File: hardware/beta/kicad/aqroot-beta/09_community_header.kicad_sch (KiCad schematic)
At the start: 0 parts

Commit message: AQROOT Beta: finish power-tree integration and add community-header connector map
01_POWER_TREE:
- Wire MAX17048 fuel gauge (U14): VDD/CELL to BAT_PROTECTED_P, GND/EP/CTG
  to GND, SCL to I2C_SCL_INT, SDA to I2C_SDA_INT, QSTRT no-connect.
- Add C36 bulk cap on BAT_PROTECTED_P and TP11 test point on MAX17048_ALRT_N.
- Add 8 hierarchical labels: USB_D_N_MCU, USB_D_P_MCU, I2C_SDA_INT,
  I2C_SCL_INT, NFC_5V_EN, NFC_5V_PA_PENDING, BQ25185_SYS, BAT_PROTECTED_P.

Root sheet:
- Import the 8 matching 01_POWER_TREE sheet pins and name six of them at
  root level, promoting BQ25185_SYS, BAT_PROTECTED_P, NFC_5V_EN,
  USB_D_N_MCU and USB_D_P_MCU from sheet-local to root nets.

09_COMMUNITY_HEADER:
- Add J5 (Conn_02x13_Odd_Even, PinHeader_2x13_P2.54mm_Vertical) with the
  full 26-pin map, plus orientation and 3.3V-only warning notes.

04_SPI_B_RADIOS_NFC:
- KiCad de-duplicated two colliding pin UUIDs on C19 (the file carried each
  UUID twice); included because it is a file-integrity fix, no design change.

Known incomplete, carried forward:
- Root sheet pins I2C_SDA_INT and NFC_5V_PA_PENDING are imported but not
  wired, so MAX17048 SDA sits on an isolated sheet-local net while SCL is
  bonded. Fuel-gauge I2C is not yet electrically complete.
- Community header nets are sheet-local only; 09_COMMUNITY_HEADER has no
  root sheet pins, and the 100R series / ESD parts named in its notes do
  not exist yet.
- Not ERC-clean and not fabrication-ready.

Co-Authored-By: Claude Opus 5 <noreply@anthropic.com>
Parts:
- added J5: COMMUNITY_HEADER_2x13, Connector_PinHeader_2.54mm:PinHeader_2x13_P2.54mm_Vertical, symbol Connector_Generic:Conn_02x13_Odd_Even
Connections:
- new net +3V3: J5.1 (Pin_1)
- new net ACC_3V3_SW: J5.26 (Pin_26)
- new net FAST_IO_GPIO43_HDR: J5.23 (Pin_23)
- new net GND: J5.13 (Pin_13), J5.2 (Pin_2), J5.20 (Pin_20), J5.25 (Pin_25), J5.7 (Pin_7)
- new net I2C_SCL_EXT_HDR: J5.22 (Pin_22)
- new net I2C_SDA_EXT_HDR: J5.21 (Pin_21)
- new net WAKE_ATTN_N_HDR: J5.24 (Pin_24)
- new net XGPIO0_HDR: J5.3 (Pin_3)
- new net XGPIO10_HDR: J5.15 (Pin_15)
- new net XGPIO11_HDR: J5.16 (Pin_16)
- new net XGPIO12_HDR: J5.17 (Pin_17)
- new net XGPIO13_HDR: J5.18 (Pin_18)
- new net XGPIO14_HDR: J5.19 (Pin_19)
- new net XGPIO1_HDR: J5.4 (Pin_4)
- new net XGPIO2_HDR: J5.5 (Pin_5)
- new net XGPIO3_HDR: J5.6 (Pin_6)
- new net XGPIO4_HDR: J5.8 (Pin_8)
- new net XGPIO5_HDR: J5.9 (Pin_9)
- new net XGPIO6_HDR: J5.10 (Pin_10)
- new net XGPIO7_HDR: J5.11 (Pin_11)
- new net XGPIO8_HDR: J5.12 (Pin_12)
- new net XGPIO9_HDR: J5.14 (Pin_14)
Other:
- note added: "COMMUNITY HEADER - 2×13, 2.54 mm PIN 1 = +3V3 ODD PINS = LEFT COLUMN EVEN PINS = RIGHT COLUMN TOP TO BOTTOM BETA CONNECTOR IS NOT KEYED ADD PIN-1 TRIANGLE ON SILKSCREEN PRODUCTION UPGRADE: SHROUDED / KEYED CONNECTOR"
- note added: "COMMUNITY HEADER LOGIC = 3.3V ONLY NO 5V-TOLERANCE CLAIM NO 5V PASSTHROUGH ALL XGPIO LINES: 100R SERIES + CONNECTOR-SIDE ESD"

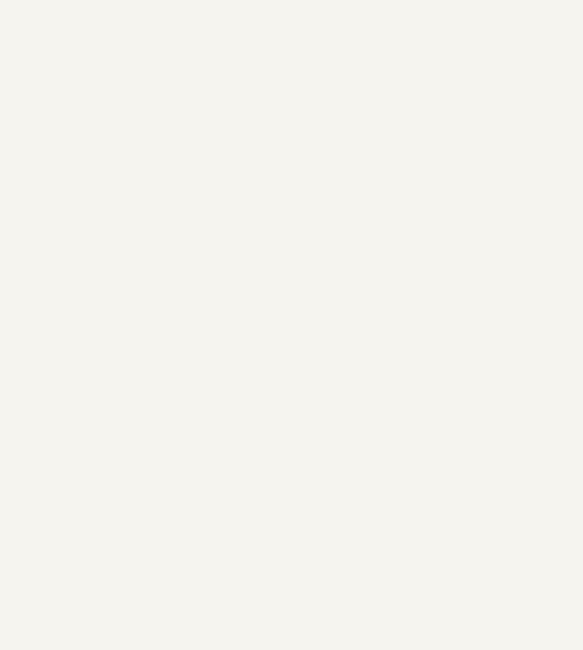
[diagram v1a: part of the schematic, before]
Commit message: AQROOT Beta: expose community-header internal hierarchy
09_COMMUNITY_HEADER:
- Add 20 hierarchical labels declaring the sheet's interface: XGPIO0-XGPIO14
  (bidirectional), I2C_SDA_INT (bidirectional), I2C_SCL_INT (input),
  ACC_PWR_EN (input), FAST_IO_U0TXD_ROOTPROBE_CS (input) and WAKE_INT_N
  (output). Purely additive: 220 insertions, 0 deletions.
- The existing connector-side local labels (XGPIO0_HDR-XGPIO14_HDR,
  I2C_SDA_EXT_HDR, I2C_SCL_EXT_HDR, FAST_IO_GPIO43_HDR, WAKE_ATTN_N_HDR,
  ACC_3V3_SW) are untouched.

Root sheet:
- Add the 20 matching sheet pins to the 09_COMMUNITY_HEADER sheet symbol.

This exposes the interface only. It does not connect anything:

- All 20 new root sheet pins are PLACED BUT UNWIRED. None carries a root
  wire, none has a matching root label, and none shares a net with any
  other sheet pin. Root pins still require wiring.
- The 20 new hierarchical labels inside 09 are likewise not attached to any
  wire, so they do not yet meet the *_HDR connector nets.
- J5 protection circuitry is not captured yet. The sheet notes call for
  100R series resistors and connector-side ESD on every XGPIO line; those
  parts do not exist, and they are what should eventually bridge XGPIO<n>
  to XGPIO<n>_HDR.

Verified with kicad-cli netlist export: this commit changes zero
connectivity. 145 nets and 433 pins before and after, with no pin changing
net. ERC rises 217 -> 257 violations, exactly +20 pin_not_connected and
+20 label_dangling, one of each per declared signal.

Not ERC-clean. Not fabrication-ready.

Co-Authored-By: Claude Opus 5 <noreply@anthropic.com>
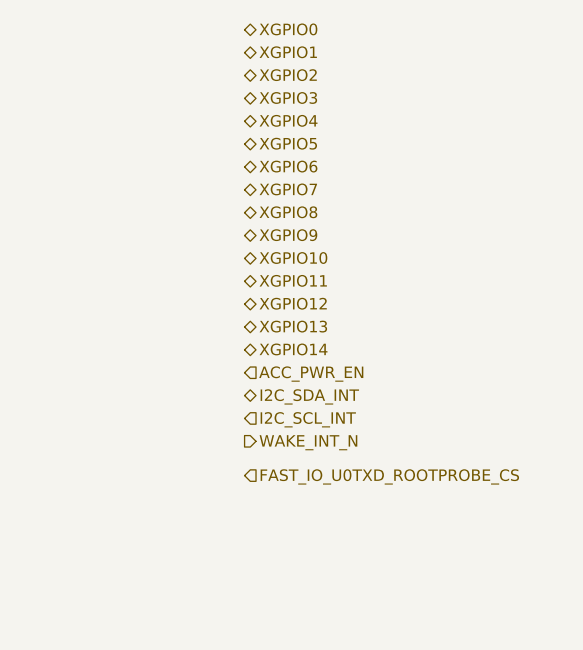
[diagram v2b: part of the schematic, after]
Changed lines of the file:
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@@
+		)
+	)
+	(hierarchical_label "XGPIO6"
+		(shape bidirectional)
+		(at 251.46 44.45 0)
+		(effects
+			(font
+				(size 1.27 1.27)
+			)
+			(justify left)
+		)
+	)
+	(hierarchical_label "XGPIO11"
+		(shape bidirectional)
+		(at 251.46 57.15 0)
+		(effects
+			(font
+				(size 1.27 1.27)
+			)
+			(justify left)
+		)
+	)
+	(hierarchical_label "I2C_SCL_INT"
+		(shape input)
+		(at 251.46 72.39 0)
+		(effects
+			(font
+				(size 1.27 1.27)
+			)
+			(justify left)
+		)
+	)
+	(hierarchical_label "XGPIO1"
+		(shape bidirectional)
+		(at 251.46 31.75 0)
+		(effects
+			(font
+				(size 1.27 1.27)
+			)
+			(justify left)
+		)
+	)
+	(hierarchical_label "XGPIO8"
+		(shape bidirectional)
+		(at 251.46 49.53 0)
+		(effects
+			(font
+				(size 1.27 1.27)
+			)
+			(justify left)
+		)
+	)
+	(hierarchical_label "XGPIO13"
+		(shape bidirectional)
+		(at 251.46 62.23 0)
+		(effects
+			(font
+				(size 1.27 1.27)
+			)
+			(justify left)
+		)
+	)
+	(hierarchical_label "I2C_SDA_INT"
+		(shape bidirectional)
+		(at 251.46 69.85 0)
+		(effects
+			(font
+				(size 1.27 1.27)
+			)
+			(justify left)
+		)
+	)
+	(hierarchical_label "XGPIO7"
+		(shape bidirectional)
+		(at 251.46 46.99 0)
+		(effects
+			(font
+				(size 1.27 1.27)
+			)
+			(justify left)
+		)
+	)
+	(hierarchical_label "XGPIO2"
+		(shape bidirectional)
+		(at 251.46 34.29 0)
+		(effects
+			(font
+				(size 1.27 1.27)
+			)
+			(justify left)
+		)
+	)
+	(hierarchical_label "XGPIO0"
+		(shape bidirectional)
+		(at 251.46 29.21 0)
+		(effects
+			(font
+				(size 1.27 1.27)
+			)
+			(justify left)
+		)
+	)
+	(hierarchical_label "ACC_PWR_EN"
+		(shape input)
+		(at 251.46 67.31 0)
+		(effects
+			(font
+				(size 1.27 1.27)
+			)
+			(justify left)
+		)
+	)
+	(hierarchical_label "XGPIO10"
+		(shape bidirectional)
+		(at 251.46 54.61 0)
+		(effects
+			(font
+				(size 1.27 1.27)
+			)
+			(justify left)
+		)
+	)
+	(hierarchical_label "FAST_IO_U0TXD_ROOTPROBE_CS"
+		(shape input)
+		(at 251.46 78.74 0)
+		(effects
+			(font
+				(size 1.27 1.27)
+			)
+			(justify left)
+		)
+	)
+	(hierarchical_label "XGPIO9"
+		(shape bidirectional)
+		(at 251.46 52.07 0)
+		(effects
+			(font
+				(size 1.27 1.27)
+			)
+			(justify left)
+		)
+	)
+	(hierarchical_label "XGPIO5"
+		(shape bidirectional)
+		(at 251.46 41.91 0)
+		(effects
+			(font
+				(size 1.27 1.27)
+			)
+			(justify left)
+		)
+	)
+	(hierarchical_label "XGPIO14"
+		(shape bidirectional)
+		(at 251.46 64.77 0)
+		(effects
+			(font
+				(size 1.27 1.27)
+			)
+			(justify left)
+		)
+	)
+	(hierarchical_label "WAKE_INT_N"
+		(shape output)
+		(at 251.46 74.93 0)
+		(effects
+			(font
+				(size 1.27 1.27)
+			)
+			(justify left)
+		)
+	)
+	(hierarchical_label "XGPIO3"
+		(shape bidirectional)
+		(at 251.46 36.83 0)
+		(effects
+			(font
+				(size 1.27 1.27)
+			)
+			(justify left)
+		)
+	)
+	(hierarchical_label "XGPIO12"
+		(shape bidirectional)
+		(at 251.46 59.69 0)
+		(effects
+			(font
+				(size 1.27 1.27)
+			)
+			(justify left)
+		)
+	)
+	(hierarchical_label "XGPIO4"
+		(shape bidirectional)
+		(at 251.46 39.37 0)
+		(effects
+			(font
+				(size 1.27 1.27)
+			)
+			(justify left)
 		)
 	)

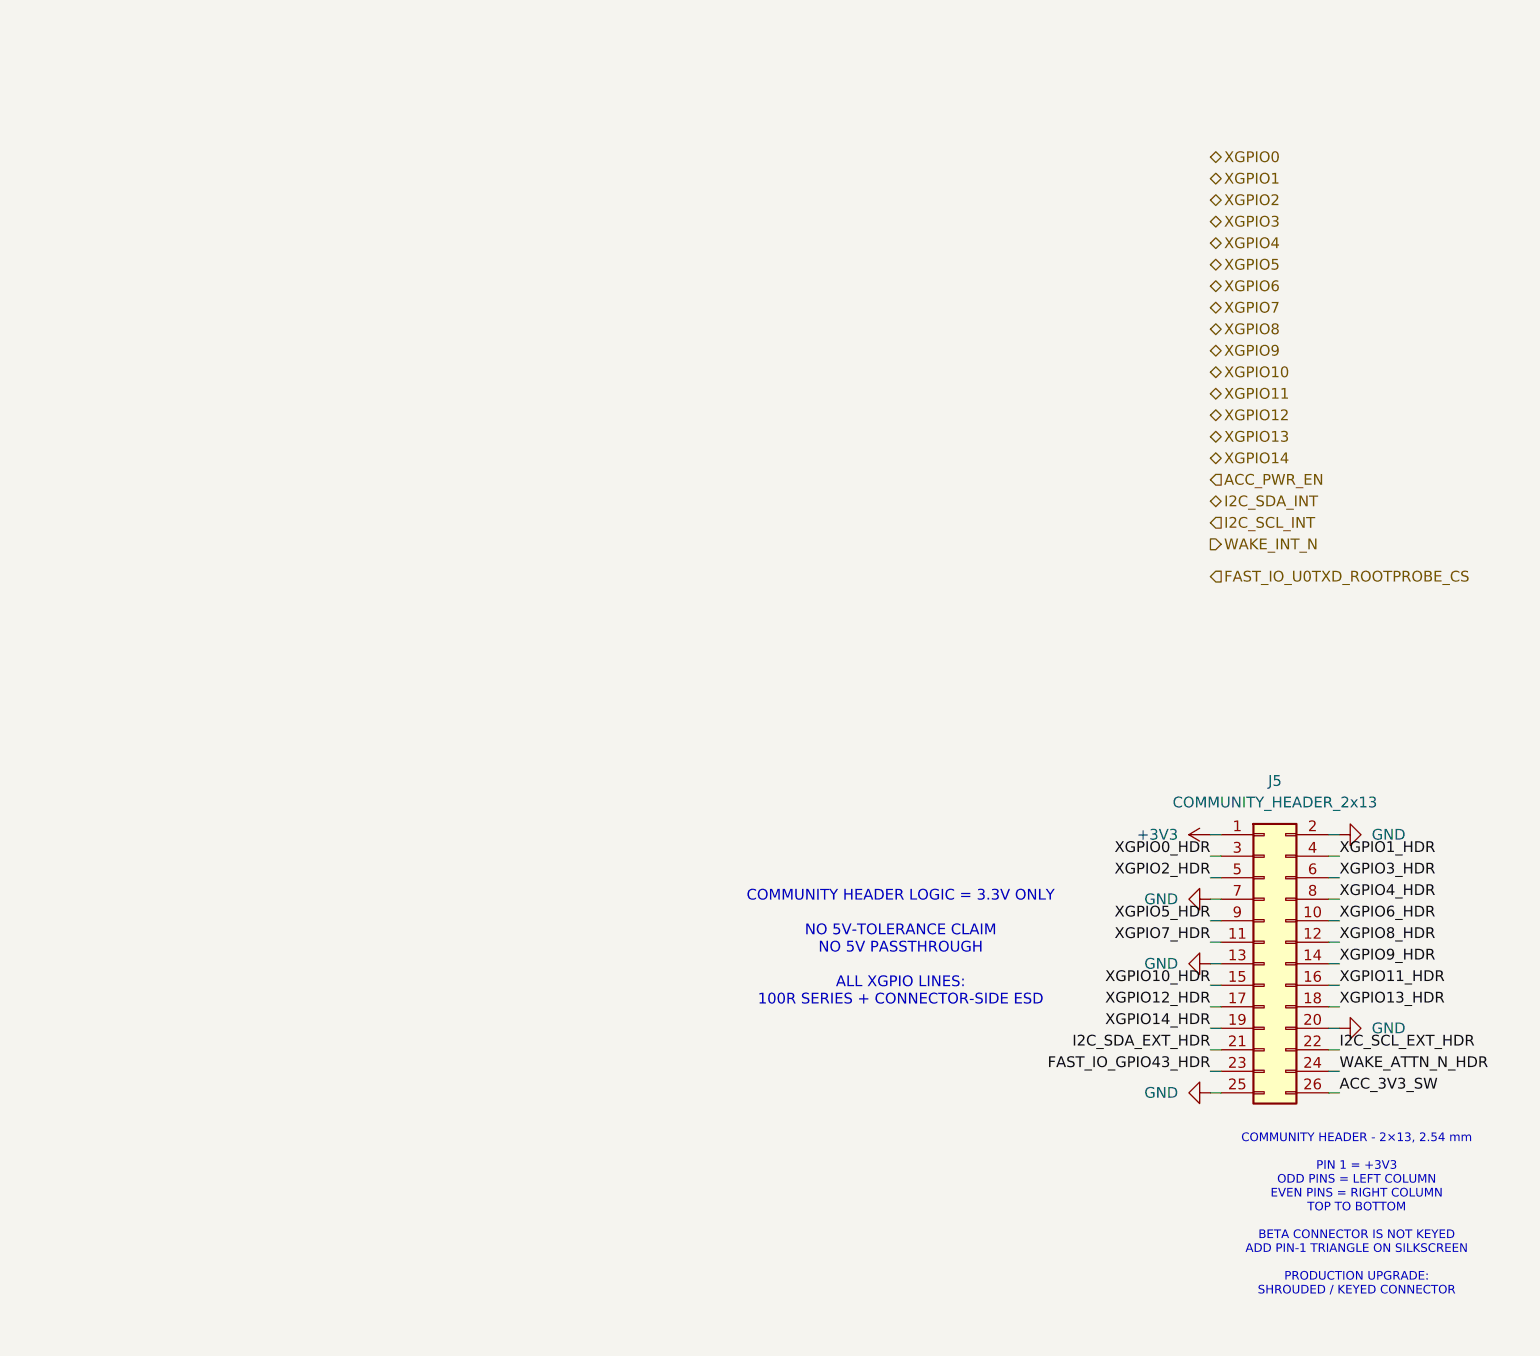
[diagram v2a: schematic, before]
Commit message: AQROOT Beta: add accessory power and protected external I2C
Checkpoint of the 09_COMMUNITY_HEADER accessory-power and protected external
I2C milestone. Verified with a scratch kicad-cli netlist export and ERC.

Confirmed as designed:
- TPS22918 (U15): VIN=+3V3, ON=ACC_PWR_EN, GND=GND, VOUT on the accessory rail.
  C37 1uF +3V3->GND, C38 1uF rail->GND, C39 100nF CT->GND, R46 100k QOD->rail,
  TP12 on rail.
- TCA9517A (U16): VCCA=+3V3, VCCB=rail, EN=ACC_PWR_EN, SCLA=I2C_SCL_INT,
  SDAA=I2C_SDA_INT. C40 100nF +3V3->GND, C42 100nF rail->GND.
- R47 22R from SCLB to I2C_SCL_EXT_HDR; R48 22R from SDAB to I2C_SDA_EXT_HDR.
- TPD2E009DBZR (D2): IO1 on I2C_SCL_EXT_HDR, IO2 on I2C_SDA_EXT_HDR, GND on
  GND. SDA and SCL confirmed as distinct nets.
- R49 4.7k between rail and I2C_SDA_EXT_HDR; R50 4.7k between rail and
  I2C_SCL_EXT_HDR.
- The accessory rail is a single correctly wired 9-node net: U15.6, U16.8,
  C38.1, C42.2, R46.2, R49.2, R50.2, TP12.1, J5.26.

Defects found during verification, NOT fixed in this commit:
- An empty label, (label "") at (273.05, 99.06), is attached to the accessory
  rail. KiCad resolves the name to the empty string in preference to
  ACC_3V3_SW, so the rail exports as <NO NET> and the ACC_3V3_SW name does not
  exist in the netlist. ERC reports this as multiple_net_names. Wiring is
  correct; only the net name is lost.
- U16 pin 4 (GND, power input) is not connected to board GND. It reaches GND
  only through C41 in series, on the local net Net-(U16-GND) = {U16.4, C41.2}.
- R49 and R50 do not have the KiCad (dnp yes) property set. "DNP" appears only
  in their Value strings, so they are not flagged as do-not-populate.
- 12 of the 16 parts on this sheet have no footprint assigned: C37-C42, R46-R50
  and TP12. Only D2, J5, U15 and U16 are footprinted.

Known incomplete, as expected at this milestone:
- XGPIO0-14 resistor/ESD blocks not captured
- WAKE protection not captured (J5.24 sits on a local WAKE_ATTN_N_HDR net)
- FAST_IO protection not capt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
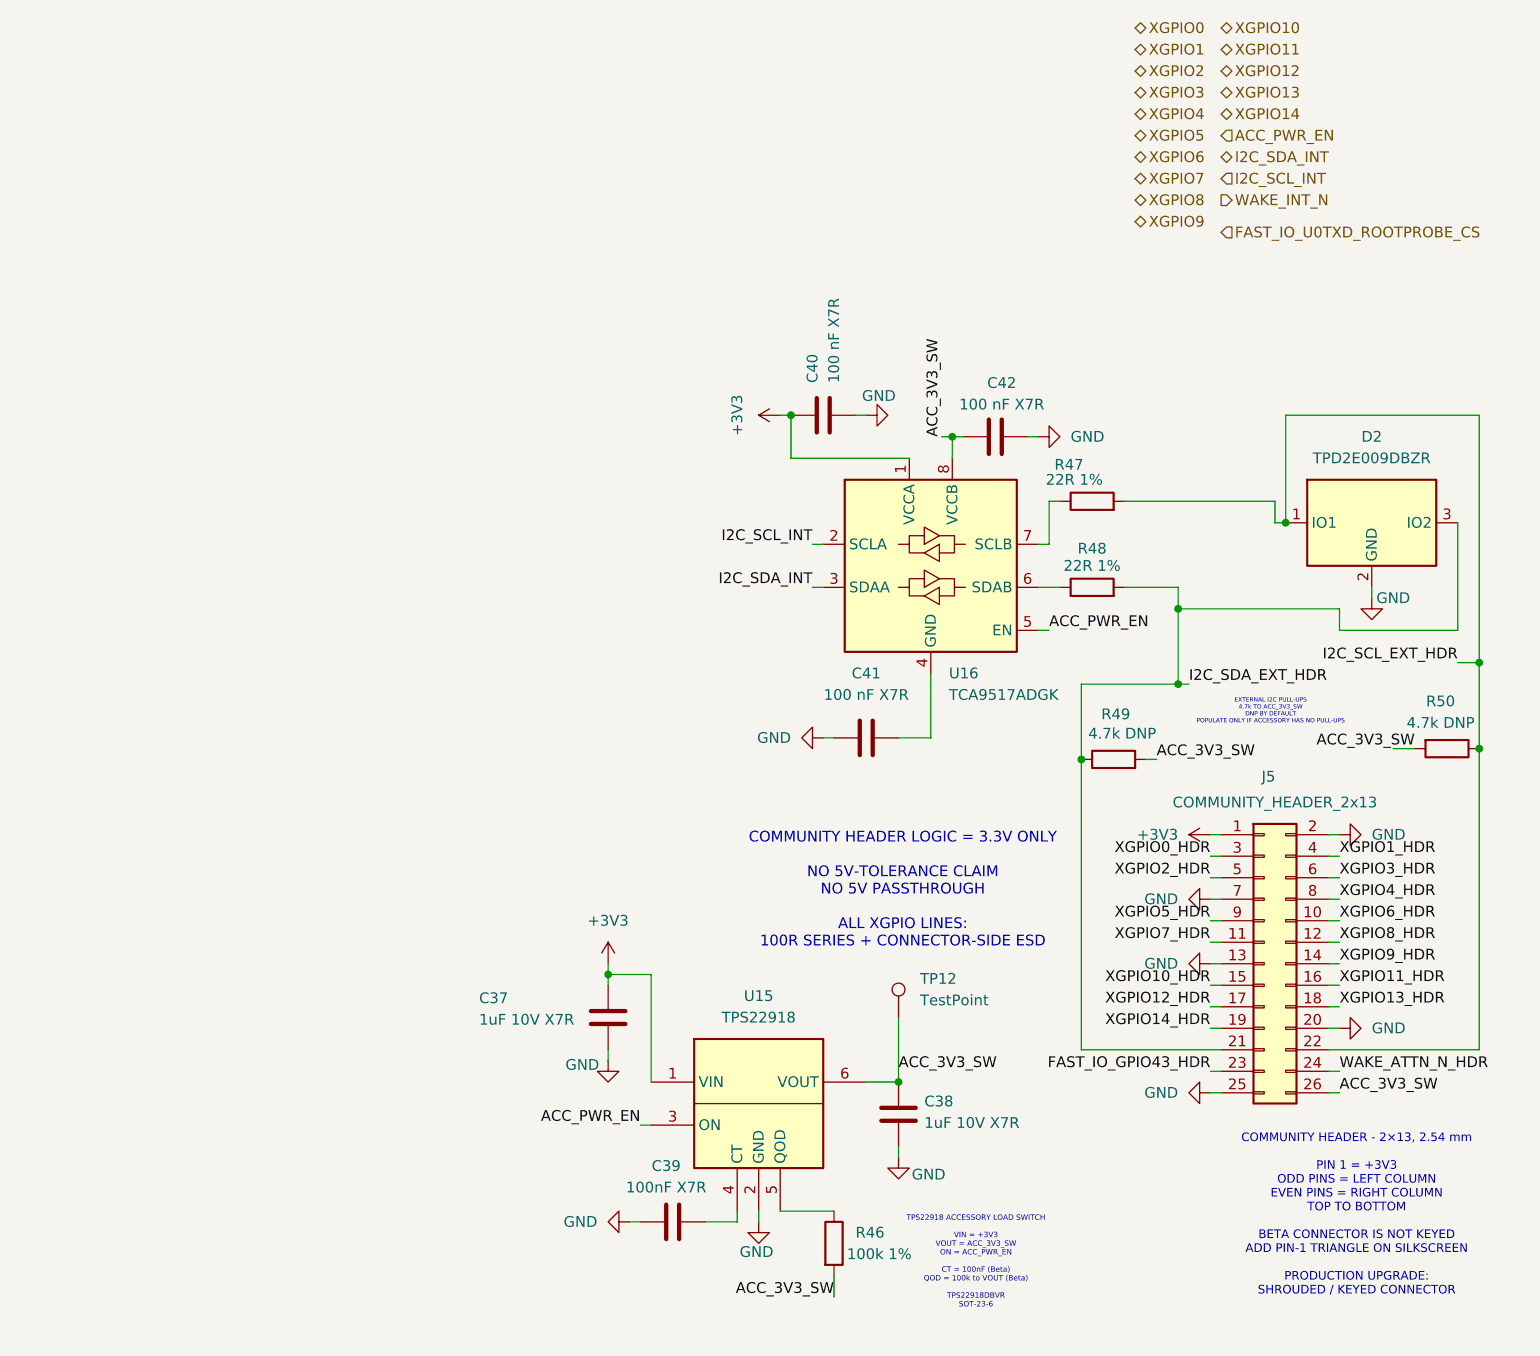
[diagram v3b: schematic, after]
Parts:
- added C37, C38: 1uF 10V X7R, symbol Device:C
- added C39: 100nF X7R, symbol Device:C
- added C40, C41, C42: 100 nF X7R, symbol Device:C
- added D2: TPD2E009DBZR, Package_TO_SOT_SMD:SOT-23, symbol AQROOT_Beta:TPD2E009DBZR
- added R46: 100k 1%, symbol Device:R
- added R47, R48: 22R 1%, symbol Device:R
- added R49, R50: 4.7k DNP, symbol Device:R
- added TP12: TestPoint, symbol Connector:TestPoint
- added U15: TPS22918, Package_TO_SOT_SMD:SOT-23-6, symbol AQROOT_Beta:TPS22918
- added U16: TCA9517ADGK, Package_SO:VSSOP-8_3x3mm_P0.65mm, symbol Logic_LevelTranslator:TCA9517ADGK
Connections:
- net +3V3: now also C37.1, C40.1, U15.1 (VIN), U16.1 (VCCA)
- net ACC_PWR_EN: now also U15.3 (ON), U16.5 (EN)
- net GND: now also C37.2, C38.2, C39.1, C40.2, C41.1, C42.1, D2.2 (GND), U15.2 (GND)
- net I2C_SCL_EXT_HDR: now also D2.1 (IO1), R47.2, R50.1
- net I2C_SCL_INT: now also U16.2 (SCLA)
- net I2C_SDA_EXT_HDR: now also D2.3 (IO2), R48.2, R49.1
- net I2C_SDA_INT: now also U16.3 (SDAA)
- net ACC_3V3_SW: no longer names the net of J5.26 (Pin_26)
- net ACC_3V3_SW: now also C38.1, C42.2, R46.2, R49.2, R50.2, TP12.1, U15.6 (VOUT), U16.8 (VCCB)
- new net: R47.1, U16.7 (SCLB)
- new net: R46.1, U15.5 (QOD)
- new net: C41.2, U16.4 (GND)
- new net: R48.1, U16.6 (SDAB)
- new net: C39.2, U15.4 (CT)
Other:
- note added: "EXTERNAL I2C PULL-UPS 4.7k TO ACC_3V3_SW DNP BY DEFAULT POPULATE ONLY IF ACCESSORY HAS NO PULL-UPS"
- note added: "TPS22918 ACCESSORY LOAD SWITCH VIN = +3V3 VOUT = ACC_3V3_SW ON = ACC_PWR_EN CT = 100nF (Beta) QOD = 100k to VOUT (Beta) TPS22918DBVR SOT-23-6"
